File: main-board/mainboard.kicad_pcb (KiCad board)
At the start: 4 copper layers, 90.2 x 95.9 mm, 269 parts, among them J1 503182-1852, J10 Conn_01x04, J11 10118194-0001LF, J12 Amphenol_901-144, J13 USB_C_Receptacle_USB2.0, J14 Conn_01x06, J15 Conn_01x02, J16 1985807, J17 1985807, J18 1985807, J2 Conn_01x05, J3 1985807, J4 1985807, J5 Amphenol_901-144, J6 Amphenol_901-144, J7 Amphenol_901-144, J8 Conn_01x09, J9 Conn_01x03, Q1 IRLML2803, Q11 MMDT2907, Q12 BSS138DWQ-7, Q13 BSS138DWQ-7, Q15 MBT2222ADW1T1, Q16 MBT2222ADW1T1, Q17 MMBT2907, Q18 BSS138DWQ-7, Q19 BSS138DWQ-7, Q2 MBT2222ADW1T1, Q20 NDS8434, Q21 NDS8434, Q22 NDS8434, Q3 MBT2222ADW1T1, Q4 IRLML2803, Q5 IRLML2803, Q6 MMBT2222AT, Q7 MBT2222ADW1T1, Q8 MBT2222ADW1T1, SW1 KMR231NG LFS, U1 MAX706RESA, U10 XTB-40, U11 XTB-40, U12 XTB-40, U13 EP2W+, U14 S1216V8, U15 RFM9xBreakout, U16 PE014006, U17 BQ25883RGER, U2 ATSAMD51J19A-AU, U21 TPS7A4501DCQT, U23 RFM98PW, U24 RFM98PW, U3 BMX160, U4 ADM1176-1ARMZ-R7, U5 TPS54226PWPRPWP14_2P31X2P46-L, U6 LTC4121, U7 KF50BD-TR, U8 MR25H40MDF, U9 XTB-40, Y1 32.768kHz

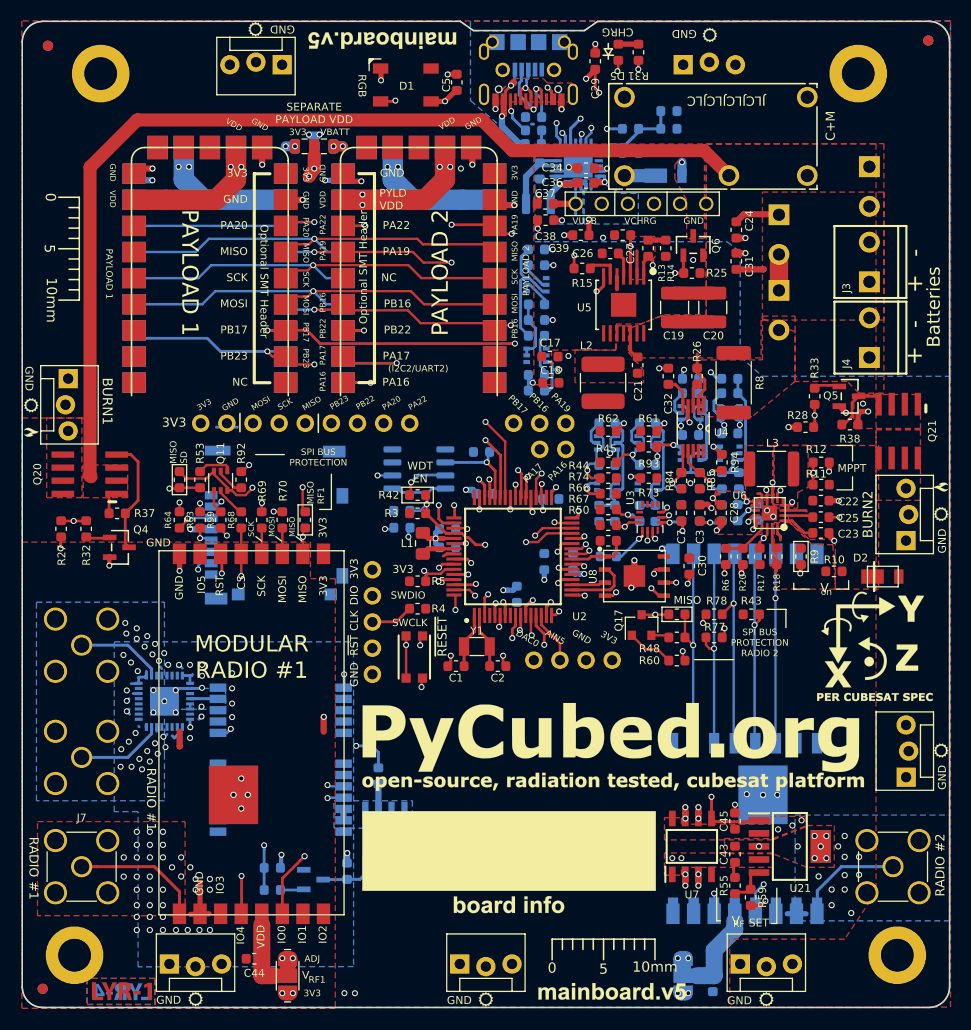
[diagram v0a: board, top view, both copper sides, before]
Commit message: added cutouts and moved SMA connection point on mainboard
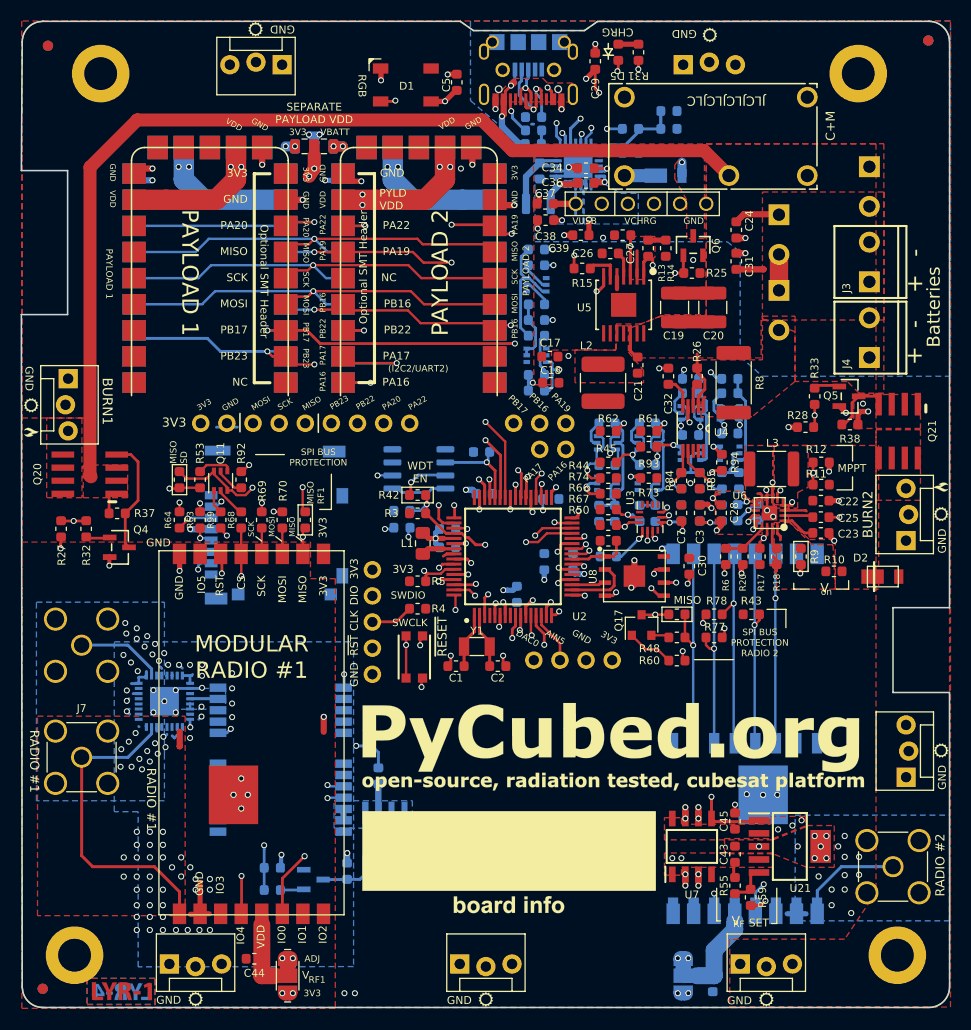
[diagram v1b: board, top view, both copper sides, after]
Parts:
- removed J5: Amphenol_901-144, Connector_Coaxial:SMA_Amphenol_901-144_Vertical
- removed the REF** at (181.2, 113.7)
- removed the REF** at (103.9, 69.6)
- removed the REF** at (155.7, 146.8)
- removed the REF** at (133.3, 54.4)
- removed the REF** at (149.9, 141.7)
- removed the REF** at (183.0, 112.3)
- removed the REF** at (132.5, 54.2)
- removed the REF** at (151.5, 146.9)
- removed the REF** at (103.9, 79.6)
- moved J7 10.6 mm to (104.1, 124.0)
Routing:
- net RF1_ANT: track 12.7 -> 22.7 mm
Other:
- board size 90.2 x 95.9 mm -> 90.3 x 95.9 mm
